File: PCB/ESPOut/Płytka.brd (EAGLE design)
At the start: 99 x 84.8 mm, 70 parts, among them IC1 L293D, IC2 LM2576S/5V, K1 G5L, K2 G5L, K3 G5L, K4 G5L, K5 G5L, Q1 AOD2922, Q2 AOD2922, Q3 AOD2922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

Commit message: no message
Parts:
- flipped C2 to the top
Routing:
- net GND: track 513.9 -> 515.4 mm
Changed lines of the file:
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@@
 <drawing>
 <settings>
-<setting alwaysvectorfont="yes"/>
+<setting alwaysvectorfont="no"/>
 <setting verticaltext="up"/>
 </settings>
@@
 <attribute name="VALUE" x="4.318" y="5.588" size="1.27" layer="27" ratio="10" rot="R270"/>
 </element>
-<element name="C2" library="rcl" library_urn="urn:adsk.eagle:library:334" package="E2,5-6" package3d_urn="urn:adsk.eagle:package:23349/1" value="" x="29.21" y="7.62" smashed="yes" rot="MR270">
-<attribute name="NAME" x="27.686" y="4.953" size="1.27" layer="26" ratio="10" rot="MR270"/>
-<attribute name="POPULARITY" value="26" x="95.25" y="-20.32" size="1.778" layer="28" rot="MR270" display="off"/>
-<attribute name="SPICEPREFIX" value="C" x="95.25" y="-20.32" size="1.778" layer="28" rot="MR270" display="off"/>
-<attribute name="VALUE" x="31.877" y="4.953" size="1.27" layer="28" ratio="10" rot="MR270"/>
+<element name="C2" library="rcl" library_urn="urn:adsk.eagle:library:334" package="E2,5-6" package3d_urn="urn:adsk.eagle:package:23349/1" value="" x="29.21" y="7.62" smashed="yes" rot="R270">
+<attribute name="NAME" x="30.734" y="4.953" size="1.27" layer="25" ratio="10" rot="R270"/>
+<attribute name="POPULARITY" value="26" x="-36.83" y="-20.32" size="1.778" layer="27" rot="R270" display="off"/>
+<attribute name="SPICEPREFIX" value="C" x="-36.83" y="-20.32" size="1.778" layer="27" rot="R270" display="off"/>
+<attribute name="VALUE" x="26.543" y="4.953" size="1.27" layer="27" ratio="10" rot="R270"/>
 </element>
 <element name="D1" library="diode" library_urn="urn:adsk.eagle:library:210" package="DO214AC" package3d_urn="urn:adsk.eagle:package:43417/2" value="" x="90.17" y="59.055" smashed="yes" rot="MR0">
@@
 <wire x1="6.9977" y1="6.81355" x2="6.985" y2="6.985" width="0.3556" layer="16"/>
 <wire x1="23.38705" y1="4.60375" x2="23.495" y2="4.445" width="0.3556" layer="16"/>
-<wire x1="25.22855" y1="6.2611" x2="29.0957" y2="6.2611" width="0.3556" layer="1"/>
-<wire x1="23.5712" y1="4.60375" x2="25.22855" y2="6.2611" width="0.3556" layer="1"/>
-<wire x1="29.0957" y1="6.2611" x2="29.21" y2="6.35" width="0.3556" layer="1"/>
-<wire x1="23.5712" y1="4.60375" x2="23.495" y2="4.445" width="0.3556" layer="1"/>
-<wire x1="35.7251" y1="12.8905" x2="45.48505" y2="12.8905" width="0.3556" layer="1"/>
-<wire x1="29.27985" y1="6.44525" x2="35.7251" y2="12.8905" width="0.3556" layer="1"/>
+<wire x1="23.495" y1="4.445" x2="23.5712" y2="4.60375" width="0.3556" layer="1"/>
+<wire x1="45.48505" y1="12.8905" x2="35.7251" y2="12.8905" width="0.3556" layer="1"/>
 <wire x1="45.48505" y1="12.8905" x2="45.6438" y2="12.9794" width="0.3556" layer="1"/>
-<wire x1="29.27985" y1="6.44525" x2="29.21" y2="6.35" width="0.3556" layer="1"/>
 <wire x1="17.6784" y1="11.4173" x2="17.6784" y2="10.86485" width="0.3556" layer="1"/>
 <wire x1="16.75765" y1="12.33805" x2="17.6784" y2="11.4173" width="0.3556" layer="1"/>
@@
 <vertex x="34.925" y="102.87"/>
 </polygon>
+<wire x1="25.31745" y1="6.35" x2="29.21" y2="6.35" width="0.3556" layer="1"/>
+<wire x1="23.5712" y1="4.60375" x2="25.31745" y2="6.35" width="0.3556" layer="1"/>
+<wire x1="35.7251" y1="12.8905" x2="32.385" y2="9.5504" width="0.508" layer="1"/>
+<wire x1="32.385" y1="9.5504" x2="32.385" y2="6.985" width="0.508" layer="1"/>
+<wire x1="32.385" y1="6.985" x2="31.75" y2="6.35" width="0.508" layer="1"/>
+<wire x1="31.75" y1="6.35" x2="30.48" y2="6.35" width="0.508" layer="1"/>
+<wire x1="30.48" y1="6.35" x2="29.21" y2="6.35" width="0.6096" layer="1"/>
 </signal>
 <signal name="+5V">
@@
 <wire x1="25.4" y1="20.955" x2="26.67" y2="22.225" width="1.016" layer="1"/>
 <wire x1="29.845" y1="22.225" x2="32.385" y2="19.685" width="1.016" layer="1"/>
-<wire x1="32.385" y1="19.685" x2="32.385" y2="13.97" width="1.016" layer="1"/>
-<wire x1="29.21" y1="10.795" x2="29.21" y2="8.89" width="1.016" layer="1"/>
 <wire x1="19.685" y1="12.7" x2="24.13" y2="12.7" width="1.016" layer="1"/>
 <wire x1="26.67" y1="22.225" x2="29.845" y2="22.225" width="1.016" layer="1"/>
-<wire x1="32.385" y1="13.97" x2="29.21" y2="10.795" width="1.016" layer="1"/>
 <wire x1="32.385" y1="19.685" x2="34.29" y2="17.78" width="1.016" layer="1"/>
 <wire x1="34.29" y1="17.78" x2="37.97" y2="17.78" width="1.016" layer="1"/>
@@
 <wire x1="80.84185" y1="30.01645" x2="80.645" y2="29.845" width="0.3556" layer="16"/>
 <via x="84.709" y="36.27755" extent="1-16" drill="0.35"/>
+<wire x1="29.21" y1="8.89" x2="32.385" y2="12.065" width="1.016" layer="1"/>
+<wire x1="32.385" y1="12.065" x2="32.385" y2="19.685" width="1.016" layer="1"/>
 </signal>
 <signal name="SCL">

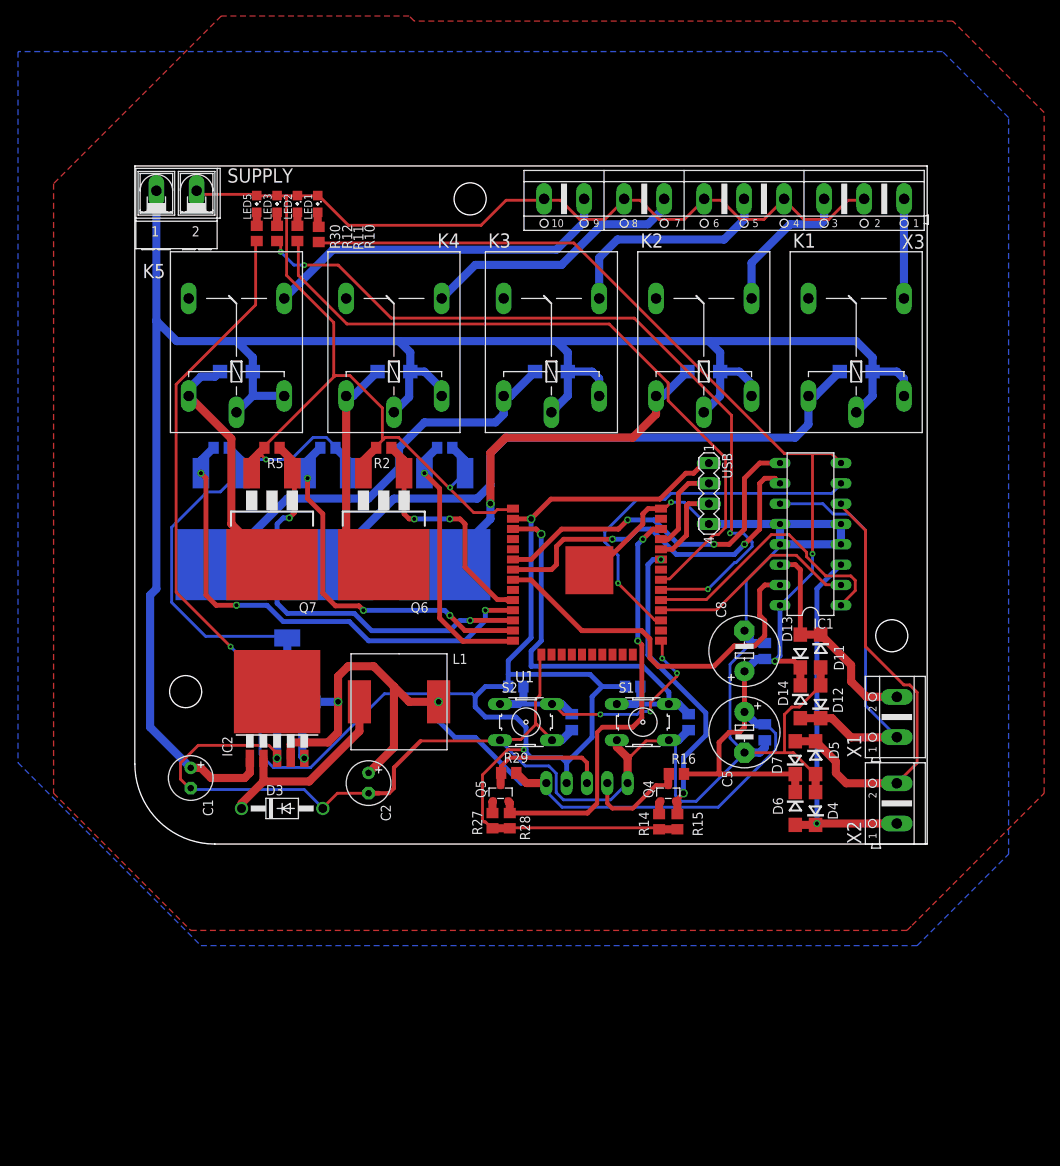
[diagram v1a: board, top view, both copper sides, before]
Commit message: Add new PCBs
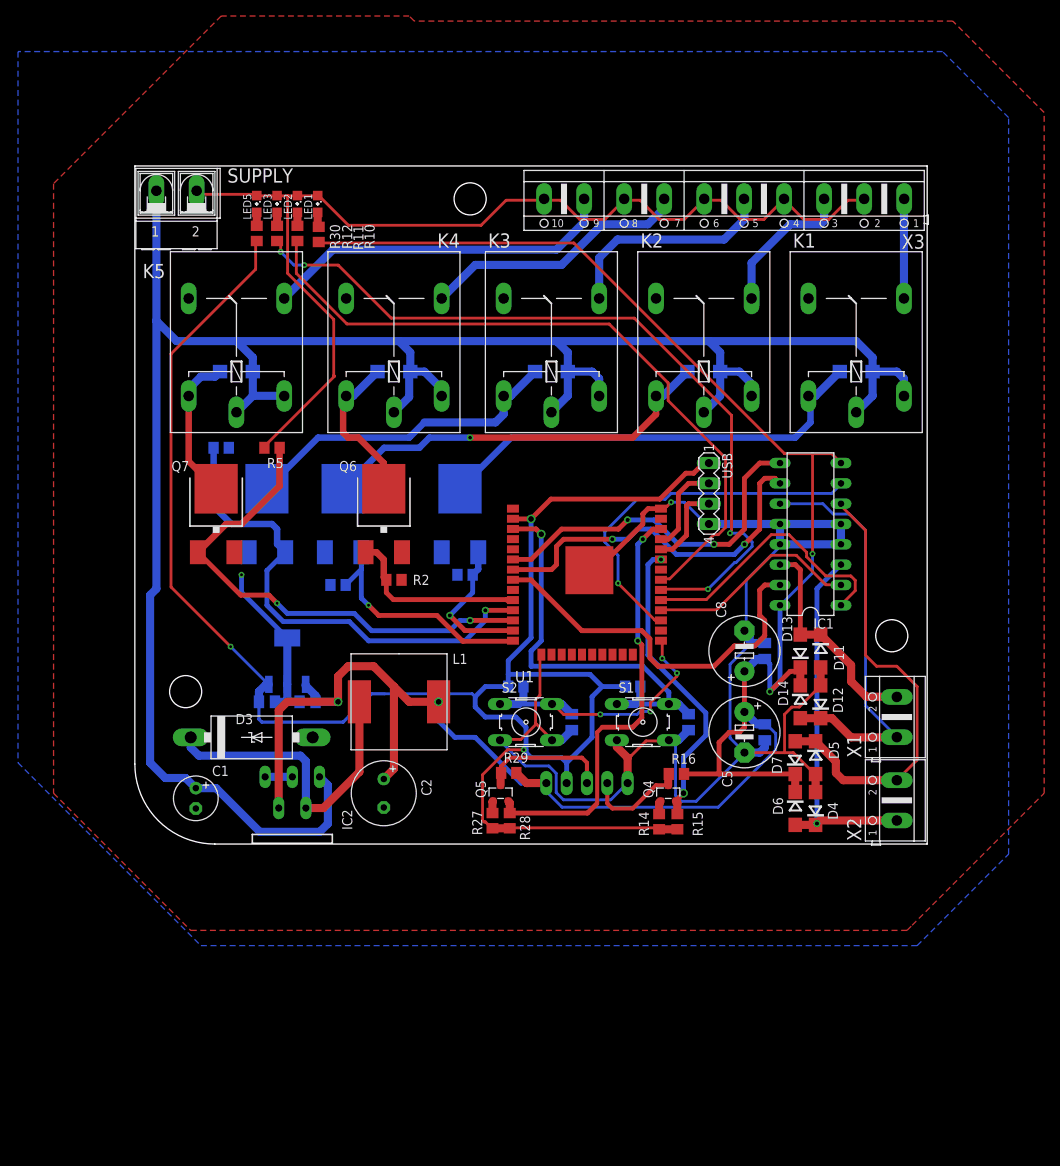
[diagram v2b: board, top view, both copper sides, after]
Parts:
- C2: device rcl:E2,5-6 -> rcl:E3,5-8
- D3: device diode:DO41-10 -> diode:C4111-15
- IC2: device v-reg-3:TO263-5 -> v-reg-3:TO220-5
- Q1, Q2, Q3, Q6, Q7: device transistor-power:D2PACK -> Clean-Kong:TO252AA
- moved R3 23.4 mm to (41.3, 33.7), turned to 180 degrees
- moved R4 21.7 mm to (25.4, 32.4), turned to 180 degrees
- moved IC2 16.6 mm to (19.7, 0.00), turned to 180 degrees
- moved Q1 16.6 mm to (40.6, 39.4), turned to 0 degrees
- moved R2 16.6 mm to (32.4, 33.0), turned to 180 degrees
- moved Q2 12.8 mm to (26.0, 39.4), turned to 0 degrees
- moved D3 9.67 mm to (14.6, 13.3)
- moved Q7 7.24 mm to (10.2, 39.4), turned to 0 degrees
- moved Q3 6.02 mm to (16.5, 39.4), turned to 0 degrees
- moved C1 2.62 mm to (7.62, 5.71)
- moved C2 2.29 mm to (31.1, 6.35)
- moved Q6 1.90 mm to (31.1, 39.4), turned to 0 degrees
- moved X2 0.38 mm to (95.2, 5.46)
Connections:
- net GND: now also Q1.2, Q2.2, Q3.2, Q6.2, Q7.2; no longer Q1.3, Q2.3, Q3.3, Q6.3, Q7.3
- net N$11: now also Q6.3; no longer Q6.2
- net N$12: now also Q1.3; no longer Q1.2
- net N$13: now also Q2.3; no longer Q2.2
- net N$16: now also Q7.3; no longer Q7.2
- net N$2: now also Q3.3; no longer Q3.2
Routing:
- net GND: track 515.4 -> 344.1 mm, vias 5 -> 2
- net P1: track 45.3 -> 18.0 mm, vias 3 -> 1
- net N$12: track 78.4 -> 55.8 mm
- net VCC: track 253.8 -> 273.6 mm
- net +5V: track 257.7 -> 274.2 mm
- net N$19: track 25.7 -> 39.6 mm
- net N$16: track 31.1 -> 18.7 mm
- net N$2: track 52.0 -> 40.9 mm
- net P3: track 53.0 -> 62.4 mm
- net N$11: track 28.6 -> 19.8 mm
- net P5: track 30.2 -> 23.1 mm, vias 2 -> 0
- net +3V3: track 243.3 -> 236.7 mm
- net N$13: track 46.5 -> 50.4 mm
- net P2: track 33.1 -> 29.7 mm
- net N$24: track 56.1 -> 56.7 mm
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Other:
- board text added: "A. KRUSZYNSKI"
- board text added: "C.KULCZYK"
- board text added: "SMART HOME v1.1"

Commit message: Creating charts
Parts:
- C1, C6: value (none) -> 100u
- C2, C3, C4, C5, C7, C8: value (none) -> 10u
- R1, R2, R25, R26, R3, R4, R5: value (none) -> 10K
- R10: value (none) -> 330
- R11, R12, R30: value (none) -> 100

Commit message: Add new method of controling the supply
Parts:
- removed C6: 100u, rcl:C0805K
- removed C7: 10u, rcl:C0805K
- removed U2: LM3940IMP-3.3, LM3940IMP-3.3:SOT230P700X180-4N
- added C9: (no value), rcl:C0805K
- added OK1: 4N35, optocoupler:DIL06
- added R35, R36, R6: (no value), rcl:R0805
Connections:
- new net EN_5V: R35.2
- new net N$15: IC2.5, OK1.5, R6.1
- new net N$26: OK1.1, R35.1
- new net N$29: C9.2, OK1.6, R36.2
- net +3V3: no longer C7.1, U2.3
- net +5V: no longer C6.1, U2.1
- net GND: now also C9.1, OK1.2, OK1.4, R36.1; no longer C6.2, C7.2, IC2.5, U2.2, U2.4
- net VCC: now also R6.2
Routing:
- net GND: track 344.1 -> 318.9 mm, vias 2 -> 1
- net +5V: track 274.2 -> 268.7 mm
- net +3V3: track 236.7 -> 232.8 mm
